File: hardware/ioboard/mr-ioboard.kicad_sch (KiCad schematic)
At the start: 131 parts, among them J1 Conn_01x40_Shielded, J2 USB_C_Receptacle_USB2.0, J3 Conn_01x06, J4 Micro_SD_Card_Det, J5 Conn_01x04, J6 Conn_01x02, Q1 2N7002, SW1 SW_Push, U1 TPS62822, U10 F1C200S, U11 TPS54202DDC, U2 TPS56637, U3 TPD2E2U06, U4 DS90C363, U5 TPD2E2U06, U6 LD3985M28R_SOT23, U7 TPS62822, U8 FUSB302BMPX, U9 TPD2E2U06, Y1 24MHz

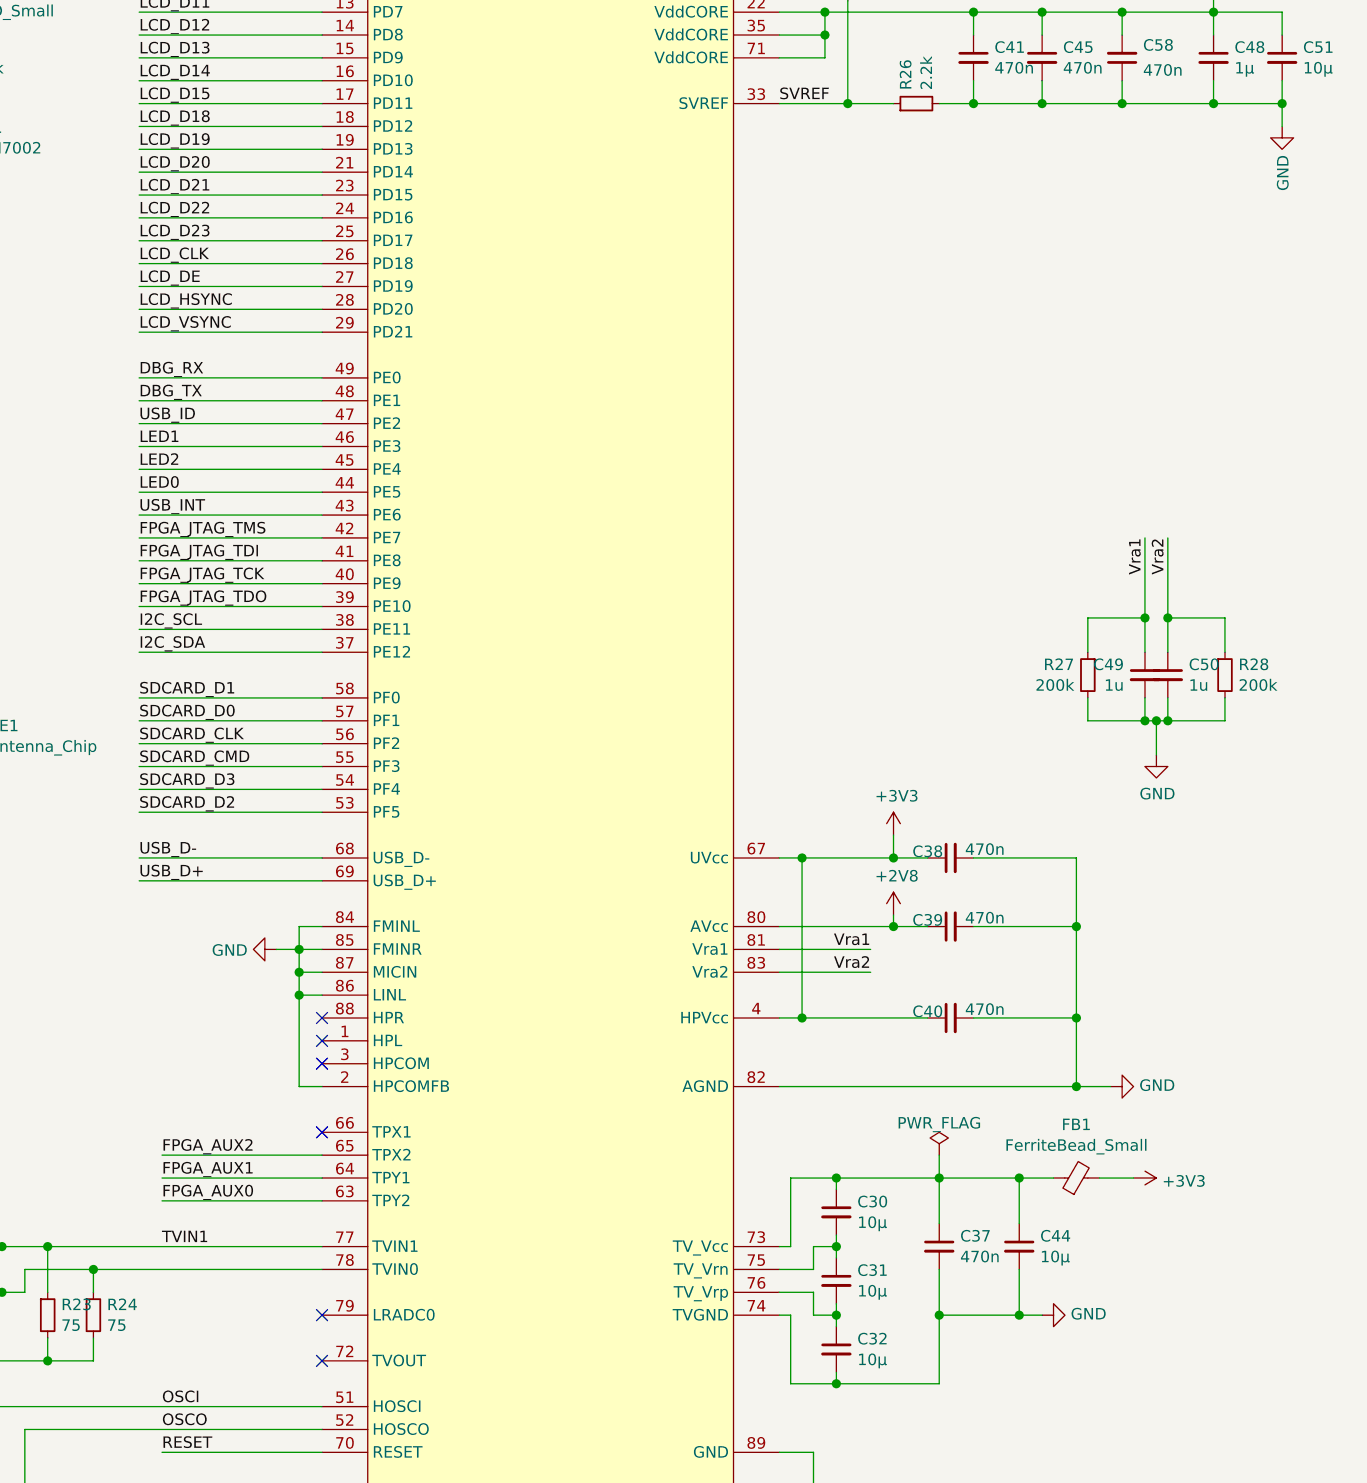
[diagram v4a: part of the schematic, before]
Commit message: Add LRADC buttons to IO board
Signed-off-by: gatecat <gatecat@ds0.me>
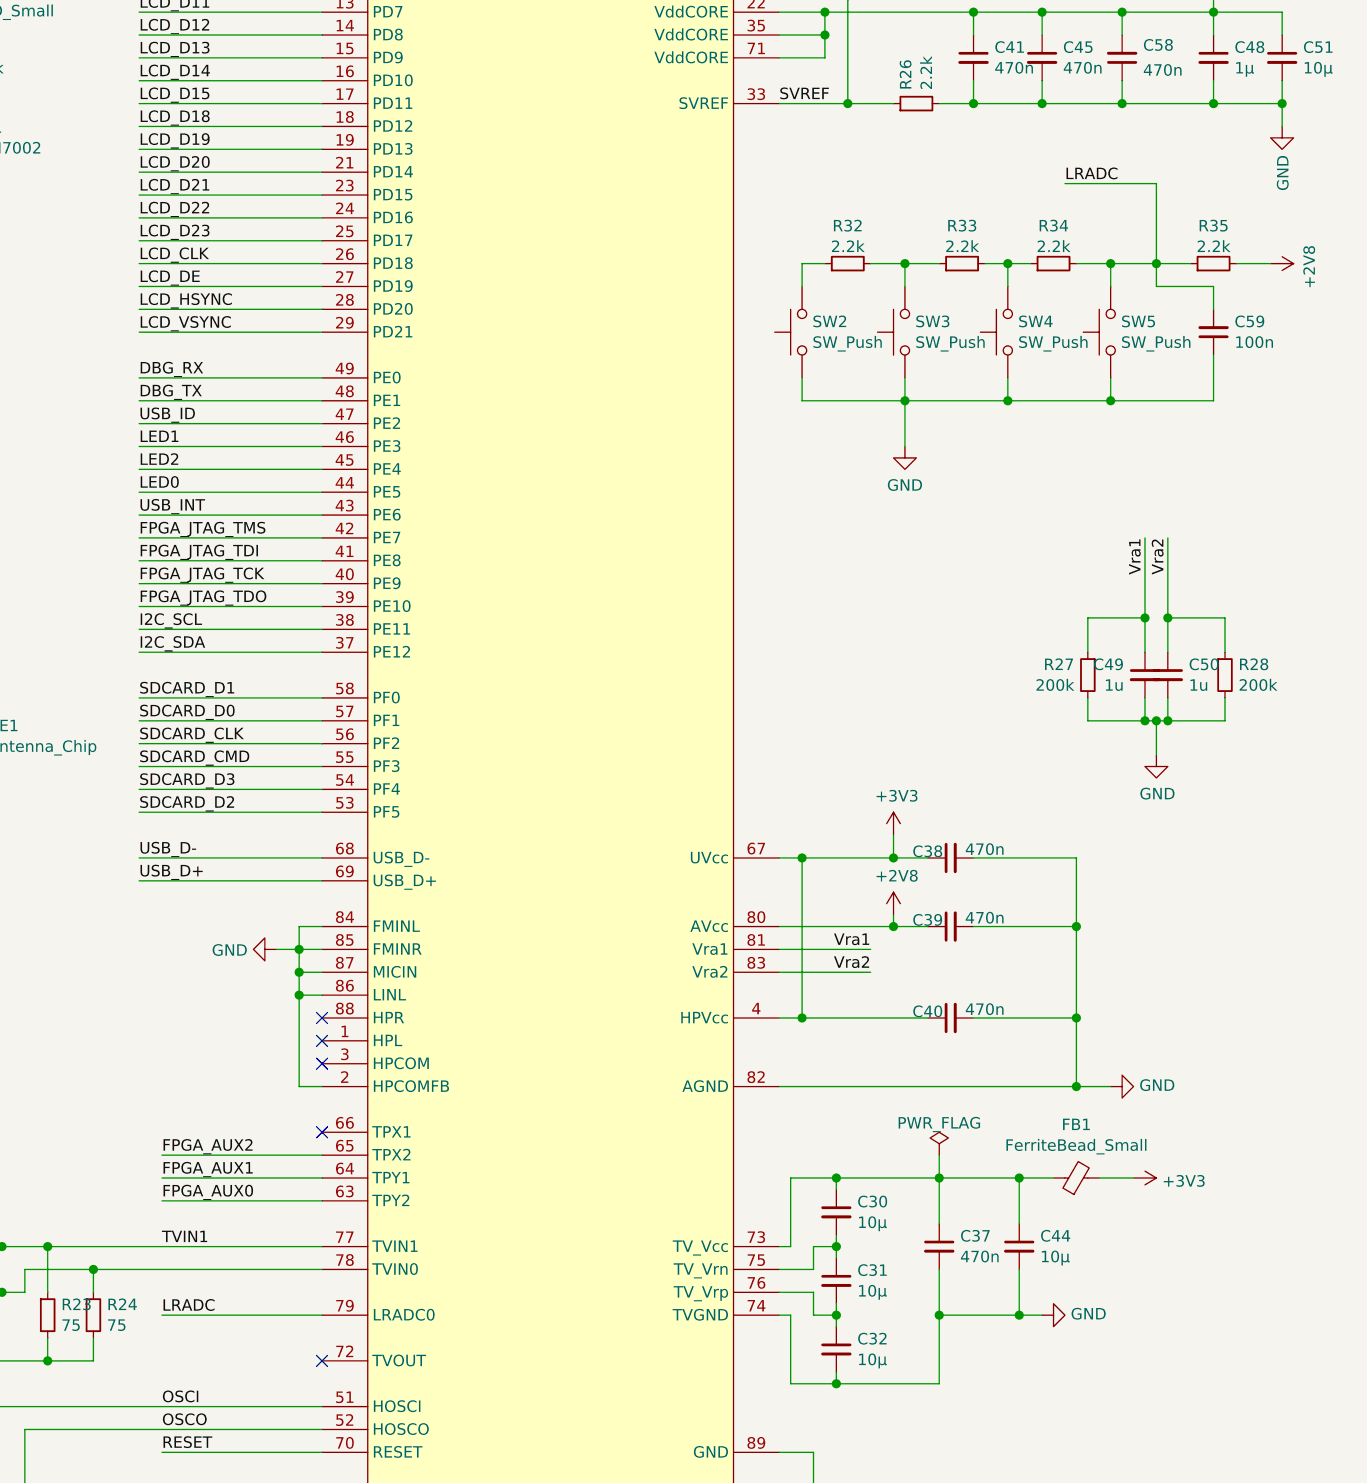
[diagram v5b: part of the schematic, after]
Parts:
- added C59: 100n, Capacitor_SMD:C_0402_1005Metric, symbol Device:C_Small
- added R32, R33, R34, R35: 2.2k, Resistor_SMD:R_0402_1005Metric, symbol Device:R_Small
- added SW2, SW3, SW4, SW5: SW_Push, Button_Switch_SMD:SW_SPST_B3U-3000P, symbol Switch:SW_Push
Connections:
- net +2V8: now also R35.2
- net GND: now also C59.1, SW2.1, SW3.1, SW4.1, SW5.1
- net LRADC: now reaches U10.79 (LRADC0)
- net LRADC: now also C59.2, R34.2, R35.1, SW5.2
- new net: R32.2, R33.1, SW3.2
- new net: R33.2, R34.1, SW4.2
- new net: R32.1, SW2.2
- no-connect marks 22 -> 21

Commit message: Use B3U-3000P for all buttons
Signed-off-by: gatecat <gatecat@ds0.me>
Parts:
- SW1: footprint Button_Switch_SMD:SW_SPST_B3U-1000P -> Button_Switch_SMD:SW_SPST_B3U-3000P
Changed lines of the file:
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@@
       (effects (font (size 1.27 1.27)) (justify right))
     )
-    (property "Footprint" "Button_Switch_SMD:SW_SPST_B3U-1000P" (id 2) (at 107.95 231.14 0)
+    (property "Footprint" "Button_Switch_SMD:SW_SPST_B3U-3000P" (id 2) (at 107.95 231.14 0)
       (effects (font (size 1.27 1.27)) hide)
     )
@@
     )
     (path "/72e45b81-c1c3-4f34-bbf4-ae3166fb09d8"
-      (reference "SW1") (unit 1) (value "SW_Push") (footprint "Button_Switch_SMD:SW_SPST_B3U-1000P")
+      (reference "SW1") (unit 1) (value "SW_Push") (footprint "Button_Switch_SMD:SW_SPST_B3U-3000P")
     )
     (path "/9802de61-b7ba-4ff6-ad97-701b5ee1b3c3"

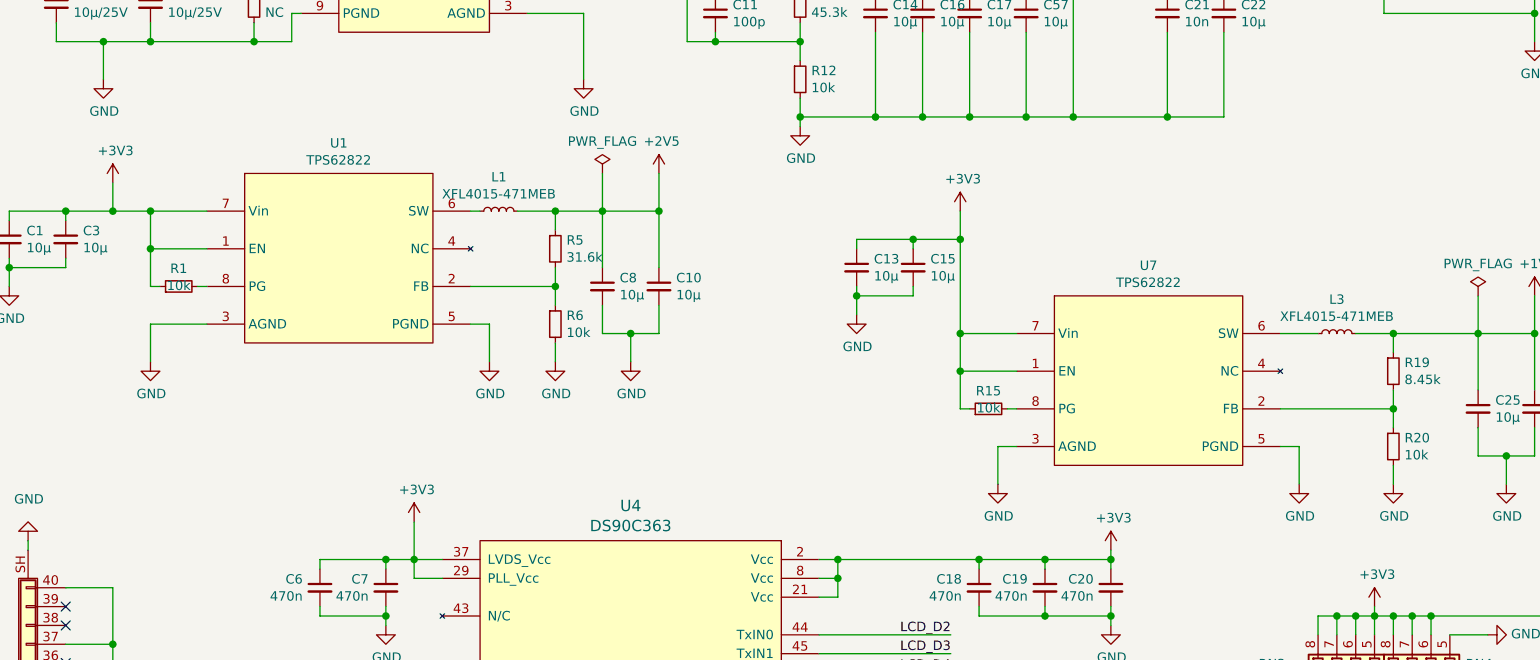
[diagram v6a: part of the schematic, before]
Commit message: Replace TPS62823  with AP3402 in schematics due to supply issues
Signed-off-by: gatecat <gatecat@ds0.me>
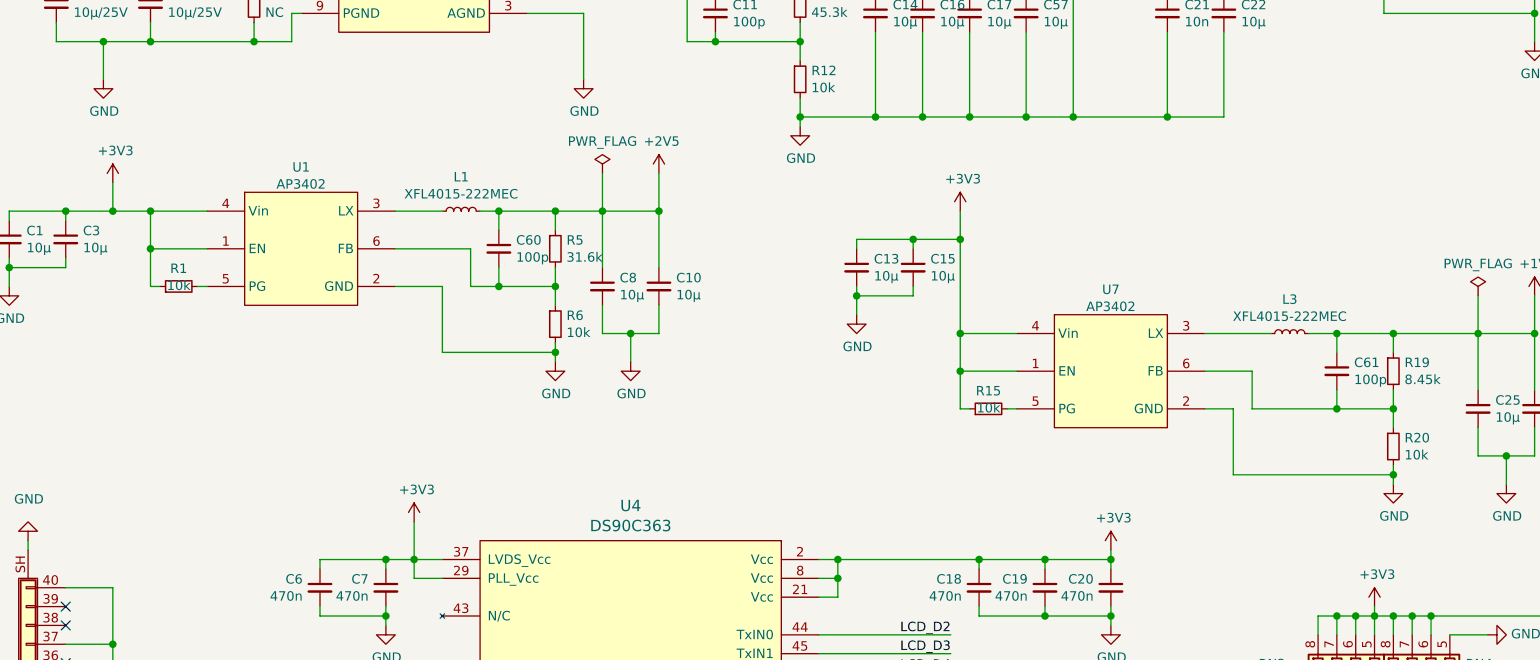
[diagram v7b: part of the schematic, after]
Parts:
- removed U1, U7: TPS62822, meowality:TI_VSON-HR_1.5x2mm_p0.5mm, symbol meowality:TPS62823
- added C60, C61: 100p, Capacitor_SMD:C_0402_1005Metric, symbol Device:C_Small
- added U1, U7: AP3402, Package_TO_SOT_SMD:TSOT-23-6, symbol meowality:AP3402
- L1, L3: value XFL4015-471MEB -> XFL4015-222MEC
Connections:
- net +1V1: now also C61.1
- net +2V5: now also C60.1
- net +3V3: now also U1.1 (EN), U1.4 (Vin), U7.1 (EN), U7.4 (Vin)
- net GND: now also U1.2 (GND), U7.2 (GND)
- net at L3.1: now also U7.3 (LX)
- net at R1.2: now also U1.5 (PG)
- net at R5.2, R6.1: now also C60.2, U1.6 (FB)
- net at R15.2: now also U7.5 (PG)
- net at R19.2, R20.1: now also C61.2, U7.6 (FB)
- net at L1.1: now also U1.3 (LX)
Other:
- moved on the sheet: L1, L3

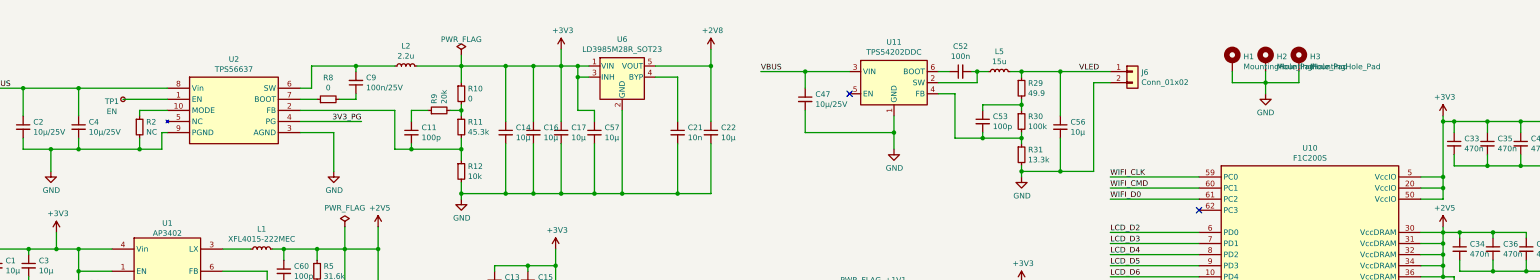
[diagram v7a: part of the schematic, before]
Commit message: Replace Vbus regs with AP64501 in schematics due to supply issues
Signed-off-by: gatecat <gatecat@ds0.me>
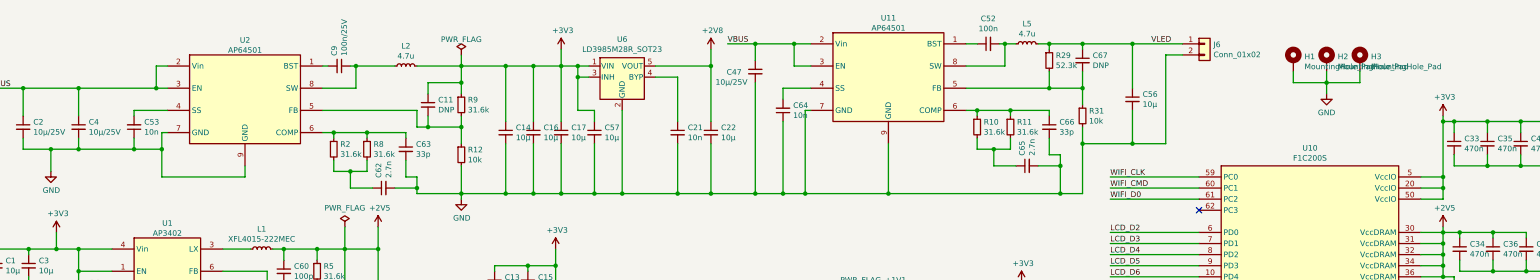
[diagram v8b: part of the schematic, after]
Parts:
- removed R30: 100k, Resistor_SMD:R_0402_1005Metric, symbol Device:R_Small
- removed TP1: EN, TestPoint:TestPoint_Pad_D2.0mm, symbol Connector:TestPoint_Small
- removed U11: TPS54202DDC, Package_TO_SOT_SMD:SOT-23-6, symbol Regulator_Switching:TPS54202DDC
- removed U2: TPS56637, meowality:VQFN10-HR, symbol meowality:TPS56637
- added C62, C65: 2.7n, Capacitor_SMD:C_0402_1005Metric, symbol Device:C_Small
- added C63, C66: 33p, Capacitor_SMD:C_0402_1005Metric, symbol Device:C_Small
- added C64: 10n, Capacitor_SMD:C_0402_1005Metric, symbol Device:C_Small
- added C67: DNP, Capacitor_SMD:C_0402_1005Metric, symbol Device:C_Small
- added U11, U2: AP64501, Package_SO:Diodes_SO-8EP, symbol meowality:AP64501
- C11: value 100p -> DNP
- C53: value 100p -> 10n
- L2: value 2.2u -> 4.7u
- L5: value 15u -> 4.7u
- R10, R8: value 0 -> 31.6k
- R11: value 45.3k -> 31.6k
- R2: value NC -> 31.6k
- R29: value 49.9 -> 52.3k
- R31: value 13.3k -> 10k
- R9: value 20k -> 31.6k
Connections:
- net +3V3: now also C11.1, R9.1; no longer R10.1
- net GND: now also C53.1, C62.2, C63.2, C64.1, C65.2, C66.2, U11.7 (GND), U11.9 (GND), U2.7 (GND), U2.9 (GND); no longer R2.2
- net VBUS: now also U11.2 (Vin), U11.3 (EN), U2.2 (Vin), U2.3 (EN)
- net VLED: now also C67.1
- net at R31.1: now also R29.2, C67.2, U11.5 (FB); no longer C53.2
- net at C52.2, L5.1: now also U11.8 (SW)
- net at C52.1: now also U11.1 (BST)
- net at R2.1: now also R8.1, C63.1, U2.6 (COMP)
- net at C11.2, R12.1: now also R9.2, U2.5 (FB); no longer R11.2
- net at C9.1: now also L2.1, U2.8 (SW); no longer R8.2
- net at C9.2: now also U2.1 (BST); no longer L2.1
- new net: C66.1, R10.1, R11.1, U11.6 (COMP)
- new net: C53.2, U2.4 (SS)
- new net: C65.1, R10.2, R11.2
- new net: C64.2, U11.4 (SS)
- new net: C62.1, R2.2, R8.2
- no-connect marks 21 -> 20
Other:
- moved on the sheet: C11, C47, C52, C56, C9, H1, H2, H3, J6, L5, R12, R29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
